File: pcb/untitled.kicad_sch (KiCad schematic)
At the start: 49 parts, among them IC10 AD844_OPAMP_MEL, IC3 FOD814_OPTO_NOSHD, IC5 FOD814_OPTO_MEL, IC6 AD844_OPAMP_AL, IC7 FOD814_OPTO_AL, IC8 AD844_OPAMP_NOSHD, J4 Conn_01x02, U2 REF192_NOSHD, U3 REF192_AL, U4 REF192_MEL

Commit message: Added non-inverting amplifier
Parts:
- removed C19, C20, C34, C38: 0.1u, capstone:CAPC220145_88N_KEM-0.1u, symbol capstone:C0805C104K5RAC7210
- removed C21, C37: 1u, capstone:C0805-1u, symbol capstone:C0805C105Z5VACTU-1u
- removed C23, C24: 10u, capstone:T495D, symbol capstone:T495D106K035ATE300
- removed C35, C36, C39, C40: 0.22u, capstone:C0805-0.22u, symbol capstone:C0805C224M5VACTU-0.22u
- removed IC10: AD844_OPAMP_MEL, capstone:SOIC127P1032X265-16N-AD844, symbol capstone:AD844JRZ-16-REEL7
- removed IC3: FOD814_OPTO_NOSHD, capstone:SOP254P1016X385-4N-FOD, symbol capstone:FOD814SD
- removed IC5: FOD814_OPTO_MEL, capstone:SOP254P1016X385-4N-FOD, symbol capstone:FOD814SD
- removed IC8: AD844_OPAMP_NOSHD, capstone:SOIC127P1032X265-16N-AD844, symbol capstone:AD844JRZ-16-REEL7
- removed J4: Conn_01x02, Connector_PinHeader_2.54mm:PinHeader_1x02_P2.54mm_Vertical, symbol Connector_Generic:Conn_01x02
- removed J_AD1, J_AD3: Conn_01x04, Connector_PinHeader_2.54mm:PinHeader_1x04_P2.54mm_Vertical, symbol Connector_Generic:Conn_01x04
- removed R15, R19: 820, Resistor_SMD:R_0402_1005Metric, symbol Device:R
- removed R16, R20: 47, Resistor_SMD:R_0402_1005Metric, symbol Device:R
- removed R17, R18, R29, R30: 100, Resistor_SMD:R_0402_1005Metric, symbol Device:R
- removed R28, R34: 100k, Resistor_SMD:R_0402_1005Metric, symbol Device:R
- removed R31, R35: 1k, Resistor_SMD:R_0402_1005Metric, symbol Device:R
- removed U2: REF192_NOSHD, capstone:R_8_ADI-REF, symbol capstone:REF192GSZ
- removed U4: REF192_MEL, capstone:R_8_ADI-REF, symbol capstone:REF192GSZ
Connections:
- no-connect marks 39 -> 13
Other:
- note removed: "Melanin Shielded"
- note removed: "No Shield"
- note removed: "Signal Output Breakout"
- moved on the sheet: C22, C28, C29, C30, C31, C32, IC6, IC7, J_AD2, R22, R23, R24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

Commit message: changed footprints and layout
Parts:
- C22: footprint capstone:T495D -> Capacitor_SMD:C_0805_2012Metric
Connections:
- net ADC1_IN14_OPTO_F_AL: now also J_AD2.3 (Pin_3); no longer J_AD2.4 (Pin_4)
- net ADC1_IN15_OPTO_E_AL: now also J_AD2.4 (Pin_4); no longer J_AD2.3 (Pin_3)
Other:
- note added: "Test ICs"
- note removed: "Aluminum Shielded"
- moved on the sheet: J_AD2

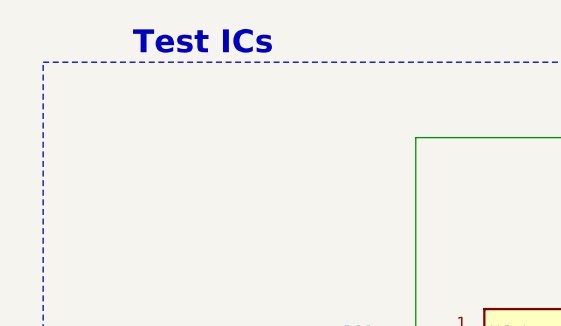
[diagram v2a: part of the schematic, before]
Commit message: Added Shields
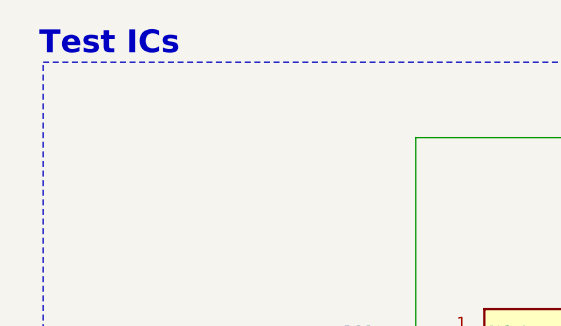
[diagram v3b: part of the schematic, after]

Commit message: Added switchable input for opto-coupler
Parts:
- added J2: Conn_01x03, Connector_PinHeader_2.54mm:PinHeader_1x03_P2.54mm_Vertical, symbol Connector_Generic:Conn_01x03
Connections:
- net +5V: now also J2.1 (Pin_1)
- net Signal Output: now also J2.3 (Pin_3); no longer R23.2
- new net: J2.2 (Pin_2), R23.2
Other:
- moved on the sheet: C22, C28, C29, C30, C31, C32, IC6, IC7, J_AD2, R22, R23, R24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
